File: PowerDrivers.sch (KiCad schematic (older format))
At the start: 58 parts, among them P2 GOOSVN, P3 GOOSVN, P4 GOOSVN, P5 GOOSVN, P6 GOOSVN, P7 GOOSVN, P8 GOOSVN, P9 GOOSVN, Q1 PSMN6R0-30YLB, Q2 PSMN6R0-30YLB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

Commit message: Finished schematics
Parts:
- removed C14: C, symbol C
- removed P3: GOOSVN, symbol CONN_01X02
- removed Q2: PSMN6R0-30YLB, symbol Q_NMOS_SSSGD
- removed R3: 470k, symbol R
- removed R5: 10k, symbol R
- added C7: 10u/25V, Capacitors_SMD:C_0805, symbol C
- added P10: GS009S, Connect:AK300-2, symbol CONN_01X02
- added Q9: PSMN6R0, SMD_Packages:SO-8_PowerPAK_Vishay_Single, symbol Q_NMOS_SSSGD
- added R18: 10k, Resistors_SMD:R_0603, symbol R
- added R4: 560k, Resistors_SMD:R_0603, symbol R
- C10, C11, C12, C13, C8, C9: value C -> 10u/25V; footprint (none) -> Capacitors_SMD:C_0805; Alt. Order Code (none) -> 302010178; Alt. Supplier (none) -> Open Parts Library; Manufacturer (none) -> Yageo; Note (none) -> 10μF/25V 0805 X5R ceramic capacitor; Order Code (none) -> 1735530; Package (none) -> 0805; Part Number (none) -> CC0805KKX5R8BB106; Supplier (none) -> Farnell
- C14: renamed from C15; footprint (none) -> Capacitors_SMD:C_0805; Alt. Order Code (none) -> 302010178; Alt. Supplier (none) -> Open Parts Library; Manufacturer (none) -> Yageo; Note (none) -> 10μF/25V 0805 X5R ceramic capacitor; Order Code (none) -> 1735530; Package (none) -> 0805; Part Number (none) -> CC0805KKX5R8BB106
- C6: renamed from C?; footprint (none) -> Capacitors_SMD:C_0603
- D1: footprint (none) -> LEDs:LED_0603; Alt. Order Code (none) -> 304090043; Alt. Supplier (none) -> Open Parts Library; Manufacturer (none) -> Everlight; Note (none) -> Green 0603 LED; Order Code (none) -> 8554609; Package (none) -> 0603
- D10, D13, D14, D2, D5, D6, D9: value LED -> LED GREEN; footprint (none) -> LEDs:LED_0603; Alt. Order Code (none) -> 304090043; Alt. Supplier (none) -> Open Parts Library; Manufacturer (none) -> Everlight; Note (none) -> Green 0603 LED; Order Code (none) -> 8554609; Package (none) -> 0603; Part Number (none) -> 19-217-G7C-AN1P2-3T; Supplier (none) -> Farnell
- D11, D12, D15, D16, D3, D4, D7, D8: footprint (none) -> Diodes_SMD:SMA_Standard; Alt. Order Code (none) -> 304020027; Alt. Supplier (none) -> Open Parts Library; Manufacturer (none) -> Diodes; Note (none) -> Schottky rectifier 40 V 1 A SOD-123; Order Code (none) -> 1773475; Package (none) -> DO-214AC; Part Number (none) -> 1N5819HW-7-F; Supplier (none) -> Farnell
- P3: renamed from P2; value GOOSVN -> GS009S; footprint (none) -> Connect:AK300-2; Alt. Order Code (none) -> 320110028; Alt. Supplier (none) -> Open Parts Library; Manufacturer (none) -> GOOSVN; Note (none) -> 5mm 2way screw terminal; Order Code (none) -> 2493622; Package (none) -> 5mm pitch; Part Number (none) -> GS009S-5.0-02P-1; Supplier (none) -> Farnell
- P4, P5, P6, P7, P8, P9: value GOOSVN -> GS009S; footprint (none) -> Connect:AK300-2; Alt. Order Code (none) -> 320110028; Alt. Supplier (none) -> Open Parts Library; Manufacturer (none) -> GOOSVN; Note (none) -> 5mm 2way screw terminal; Order Code (none) -> 2493622; Package (none) -> 5mm pitch; Part Number (none) -> GS009S-5.0-02P-1; Supplier (none) -> Farnell
- Q2: renamed from Q1; value PSMN6R0-30YLB -> PSMN6R0; footprint (none) -> SMD_Packages:SO-8_PowerPAK_Vishay_Single; Manufacturer (none) -> NXP; Note (none) -> N-channel 30V 70A LFPAK MOSFET; Order Code (none) -> 2067550; Package (none) -> Power-SO8; Part Number (none) -> PSMN6R0-30YLB
- Q3, Q4, Q5, Q6, Q7, Q8: value PSMN6R0-30YLB -> PSMN6R0; footprint (none) -> SMD_Packages:SO-8_PowerPAK_Vishay_Single; Manufacturer (none) -> NXP; Note (none) -> N-channel 30V 70A LFPAK MOSFET; Order Code (none) -> 2067550; Package (none) -> Power-SO8; Part Number (none) -> PSMN6R0-30YLB
- R10, R14, R6: value 470k -> 10k; footprint (none) -> Resistors_SMD:R_0603; Alt. Order Code (none) -> 301010299; Alt. Supplier (none) -> Open Parts Library; Manufacturer (none) -> Yageo; Note (none) -> 10kΩ/1% 0603 resistor; Order Code (none) -> 9238603; Package (none) -> 0603; Part Number (none) -> RC0603FR-0710KL; Supplier (none) -> Farnell
- R11, R15, R7: value 470k -> 560k; footprint (none) -> Resistors_SMD:R_0603; Alt. Order Code (none) -> 301010230; Alt. Supplier (none) -> Open Parts Library; Manufacturer (none) -> Yageo; Note (none) -> 560kΩ/5% 0603 resistor; Order Code (none) -> 9233717; Package (none) -> 0603; Part Number (none) -> RC0603JR-07560KL; Supplier (none) -> Farnell
- R12, R16, R8: value 10k -> 560k; footprint (none) -> Resistors_SMD:R_0603; Alt. Order Code (none) -> 301010230; Alt. Supplier (none) -> Open Parts Library; Manufacturer (none) -> Yageo; Note (none) -> 560kΩ/5% 0603 resistor; Order Code (none) -> 9233717; Package (none) -> 0603; Part Number (none) -> RC0603JR-07560KL
- R13, R17, R9: footprint (none) -> Resistors_SMD:R_0603; Alt. Order Code (none) -> 301010299; Alt. Supplier (none) -> Open Parts Library; Manufacturer (none) -> Yageo; Note (none) -> 10kΩ/1% 0603 resistor; Order Code (none) -> 9238603; Package (none) -> 0603; Part Number (none) -> RC0603FR-0710KL
- R3: renamed from R2; value 470k -> 560k; footprint (none) -> Resistors_SMD:R_0603; Alt. Order Code (none) -> 301010230; Alt. Supplier (none) -> Open Parts Library; Manufacturer (none) -> Yageo; Note (none) -> 560kΩ/5% 0603 resistor; Order Code (none) -> 9233717; Package (none) -> 0603; Part Number (none) -> RC0603JR-07560KL; Supplier (none) -> Farnell
- R5: renamed from R4; footprint (none) -> Resistors_SMD:R_0603; Alt. Order Code (none) -> 301010299; Alt. Supplier (none) -> Open Parts Library; Manufacturer (none) -> Yageo; Note (none) -> 10kΩ/1% 0603 resistor; Order Code (none) -> 9238603; Package (none) -> 0603; Part Number (none) -> RC0603FR-0710KL
- U3: renamed from U4; footprint (none) -> Housings_SSOP:TSSOP-20_4.4x6.5mm_Pitch0.65mm; Package TSSOP-16 -> TSSOP-20

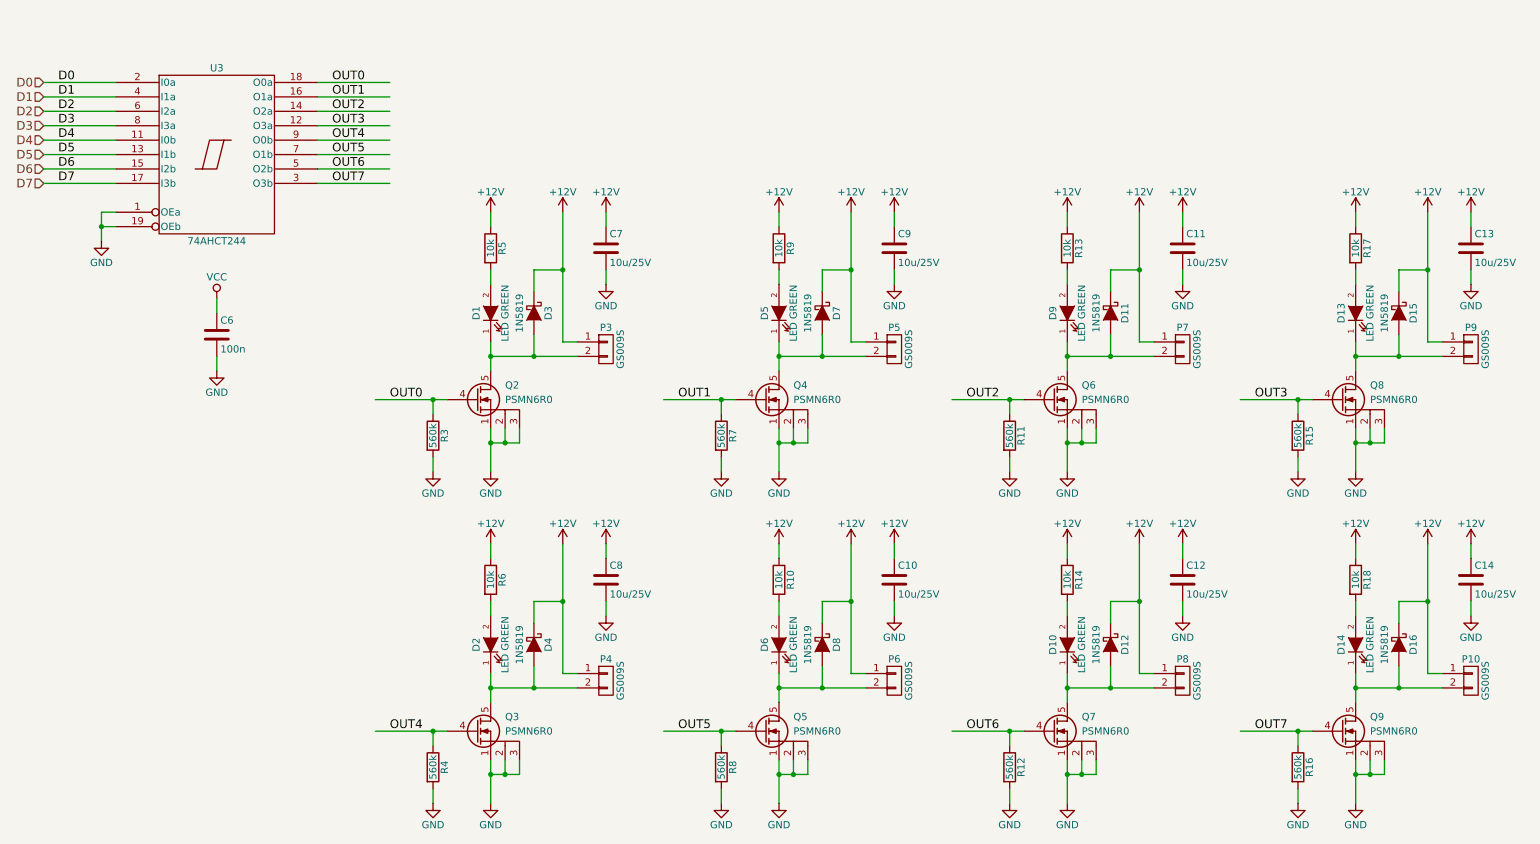
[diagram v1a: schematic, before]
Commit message: Laid out parts and routed some of the signals
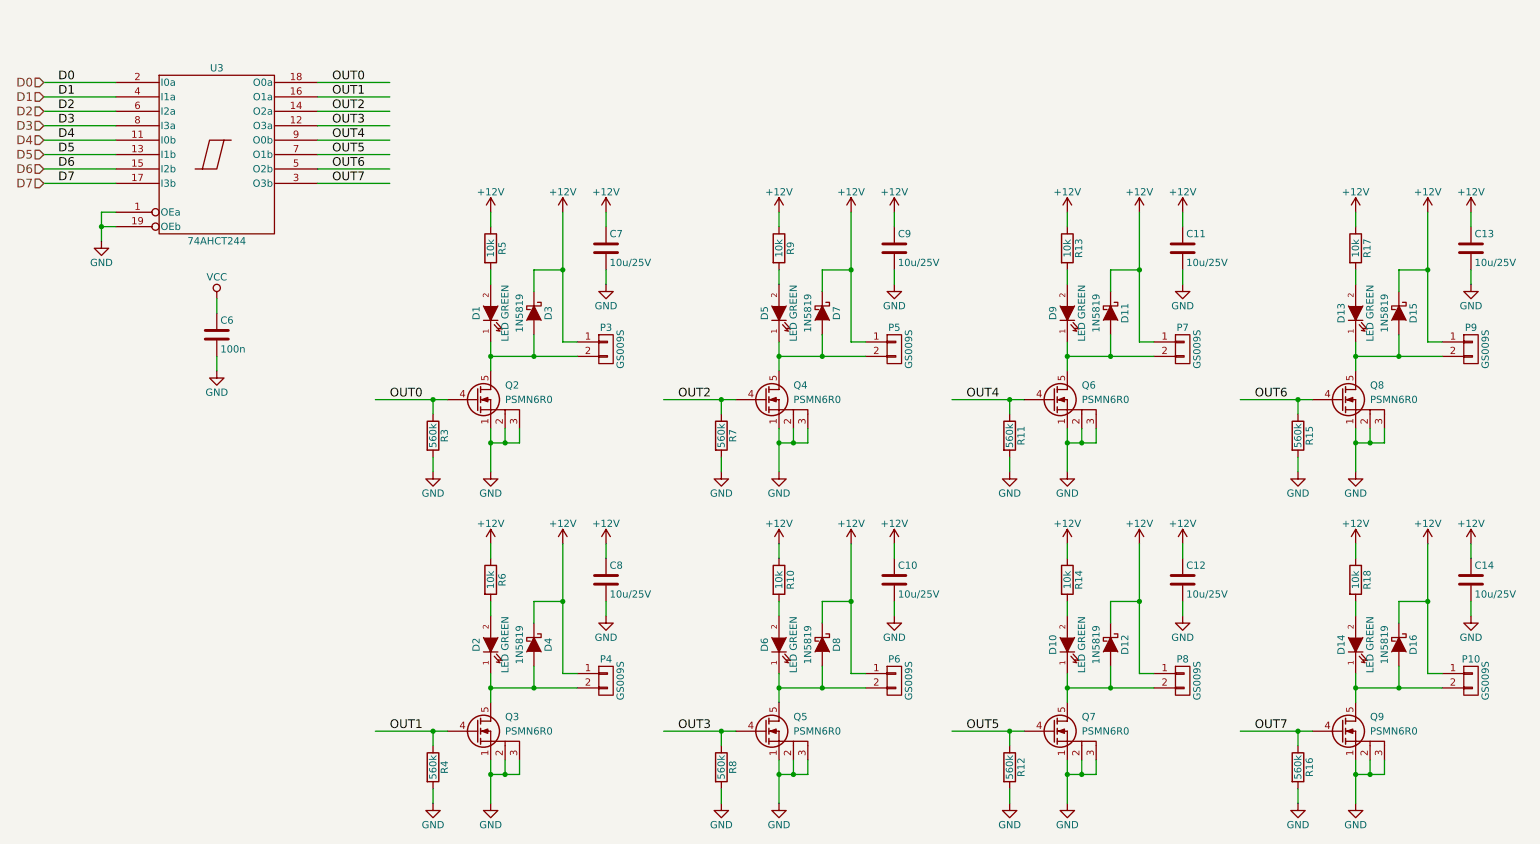
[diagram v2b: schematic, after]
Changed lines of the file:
@@
 Connection ~ 5700 3300
 Text Label 5400 3300 0    60   ~ 0
-OUT1
+OUT2
 Wire Wire Line
 	7700 3400 7700 3300
@@
 Connection ~ 7700 3300
 Text Label 7400 3300 0    60   ~ 0
-OUT2
+OUT4
 Wire Wire Line
 	9700 3400 9700 3300
@@
 Connection ~ 9700 3300
 Text Label 9400 3300 0    60   ~ 0
-OUT3
+OUT6
 Wire Wire Line
 	3700 5700 3700 5600
@@
 Connection ~ 3700 5600
 Text Label 3400 5600 0    60   ~ 0
-OUT4
+OUT1
 Wire Wire Line
 	5700 5700 5700 5600
@@
 Connection ~ 5700 5600
 Text Label 5400 5600 0    60   ~ 0
-OUT5
+OUT3
 Wire Wire Line
 	7700 5700 7700 5600
@@
 Connection ~ 7700 5600
 Text Label 7400 5600 0    60   ~ 0
-OUT6
+OUT5
 Wire Wire Line
 	9700 5700 9700 5600

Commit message: Final production board
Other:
- note added: "3.3V-TO-5V LEVEL SHIFTER"
- note added: "EIGHT INDEPENDENT HIGH-CURRENT MOSFET DRIVERS"
- note added: "POWER DRIVERS\nUp to eight external devices can be connected and controlled by the unit.\nEach device is controlled by a separate MOSFET and supplied by a 12V DC power supply.\nPWM can be employed to vary the power to the device, such as a solenoid valve or LED lightning.\nThere is a level shifter to convert the 3.3V Aurduino outputs to 5 Volts to efficiently drive the gates of the MOSFET transis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"
- moved on the sheet: C6, U3
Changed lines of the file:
@@
 LIBS:valves
 LIBS:jakub
-LIBS:garduino-cache
+LIBS:guarduino-cache
 EELAYER 25 0
 EELAYER END
@@
 encoding utf-8
 Sheet 2 4
-Title ""
-Date ""
-Rev ""
-Comp ""
-Comment1 ""
-Comment2 ""
+Title "Guarduino Control Unit"
+Date "2016-09-30"
+Rev "1.0"
+Comp "Serious Play Ltd"
+Comment1 "Jakub Nedbal"
+Comment2 "License: CC-BY-SA"
 Comment3 ""
 Comment4 ""
@@
 Connection ~ 5700 3300
 Text Label 5400 3300 0    60   ~ 0
-OUT2
+OUT1
 Wire Wire Line
 	7700 3400 7700 3300
@@
 Connection ~ 7700 3300
 Text Label 7400 3300 0    60   ~ 0
-OUT4
+OUT2
 Wire Wire Line
 	9700 3400 9700 3300
@@
 Connection ~ 9700 3300
 Text Label 9400 3300 0    60   ~ 0
-OUT6
+OUT3
 Wire Wire Line
 	3700 5700 3700 5600
@@
 Connection ~ 3700 5600
 Text Label 3400 5600 0    60   ~ 0
-OUT1
+OUT4
 Wire Wire Line
 	5700 5700 5700 5600
@@
 Connection ~ 5700 5600
 Text Label 5400 5600 0    60   ~ 0
-OUT3
+OUT5
 Wire Wire Line
 	7700 5700 7700 5600
@@
 Connection ~ 7700 5600
 Text Label 7400 5600 0    60   ~ 0
-OUT5
+OUT6
 Wire Wire Line
 	9700 5700 9700 5600
@@
 L 74LS244 U3
 U 1 1 570B4B9F
-P 2200 1600
-F 0 "U3" H 2200 2200 50  0000 C CNN
-F 1 "74AHCT244" H 2200 1000 50  0000 C CNN
-F 2 "Housings_SSOP:TSSOP-20_4.4x6.5mm_Pitch0.65mm" H 2200 1600 50  0001 C CNN
-F 3 "" H 2200 1600 50  0000 C CNN
-F 4 "SN74AHCT244PW" H 2200 1600 60  0001 C CNN "Part Number"
-F 5 "Texas Instruments" H 2200 1600 60  0001 C CNN "Manufacturer"
-F 6 "TSSOP-20" H 2200 1600 60  0001 C CNN "Package"
-F 7 "Farnell" H 2200 1600 60  0001 C CNN "Supplier"
-F 8 "9590706" H 2200 1600 60  0001 C CNN "Order Code"
-F 9 "Octal buffers/drivers with 3-state outputs" H 2200 1600 60  0001 C CNN "Note"
-	1    2200 1600
-	1    0    0    -1
-$EndComp
-Wire Wire Line
-	1500 1100 1000 1100
-Text Label 1100 1100 0    60   ~ 0
+P 2200 2400
+F 0 "U3" H 2200 3000 50  0000 C CNN
+F 1 "74AHCT244" H 2200 1800 50  0000 C CNN
+F 2 "Housings_SSOP:TSSOP-20_4.4x6.5mm_Pitch0.65mm" H 2200 2400 50  0001 C CNN
+F 3 "" H 2200 2400 50  0000 C CNN
+F 4 "SN74AHCT244PW" H 2200 2400 60  0001 C CNN "Part Number"
+F 5 "Texas Instruments" H 2200 2400 60  0001 C CNN "Manufacturer"
+F 6 "TSSOP-20" H 2200 2400 60  0001 C CNN "Package"
+F 7 "Farnell" H 2200 2400 60  0001 C CNN "Supplier"
+F 8 "9590706" H 2200 2400 60  0001 C CNN "Order Code"
+F 9 "Octal buffers/drivers with 3-state outputs" H 2200 2400 60  0001 C CNN "Note"
+	1    2200 2400
+	1    0    0    -1
+$EndComp
+Wire Wire Line
+	1500 1900 1000 1900
+Text Label 1100 1900 0    60   ~ 0
 D0
 Wire Wire Line
-	1500 1200 1000 1200
-Text Label 1100 1200 0    60   ~ 0
+	1500 2000 1000 2000
+Text Label 1100 2000 0    60   ~ 0
 D1
 Wire Wire Line
-	1500 1300 1000 1300
-Text Label 1100 1300 0    60   ~ 0
+	1500 2100 1000 2100
+Text Label 1100 2100 0    60   ~ 0
 D2
 Wire Wire Line
-	1500 1400 1000 1400
-Text Label 1100 1400 0    60   ~ 0
+	1500 2200 1000 2200
+Text Label 1100 2200 0    60   ~ 0
 D3
 Wire Wire Line
-	1500 1500 1000 1500
-Text Label 1100 1500 0    60   ~ 0
+	1500 2300 1000 2300
+Text Label 1100 2300 0    60   ~ 0
 D4
 Wire Wire Line
-	1500 1600 1000 1600
-Text Label 1100 1600 0    60   ~ 0
+	1500 2400 1000 2400
+Text Label 1100 2400 0    60   ~ 0
 D5
 Wire Wire Line
-	1500 1700 1000 1700
-Text Label 1100 1700 0    60   ~ 0
+	1500 2500 1000 2500
+Text Label 1100 2500 0    60   ~ 0
 D6
 Wire Wire Line
-	1500 1800 1000 1800
-Text Label 1100 1800 0    60   ~ 0
+	1500 2600 1000 2600
+Text Label 1100 2600 0    60   ~ 0
 D7
 Wire Wire Line
-	1500 2000 1400 2000
-Wire Wire Line
-	1400 2000 1400 2200
-Wire Wire Line
-	1400 2100 1500 2100
-Connection ~ 1400 2100
+	1500 2800 1400 2800
+Wire Wire Line
+	1400 2800 1400 3000
+Wire Wire Line
+	1400 2900 1500 2900
+Connection ~ 1400 2900
 $Comp
 L GND #PWR058
 U 1 1 570B4BBA
-P 1400 2200
-F 0 "#PWR058" H 1400 1950 50  0001 C CNN
-F 1 "GND" H 1400 2050 50  0000 C CNN
-F 2 "" H 1400 2200 50  0000 C CNN
-F 3 "" H 1400 2200 50  0000 C CNN
-	1    1400 2200
-	1    0    0    -1
-$EndComp
-Wire Wire Line
-	3400 1100 2900 1100
-Text Label 3000 1100 0    60   ~ 0
+P 1400 3000
+F 0 "#PWR058" H 1400 2750 50  0001 C CNN
+F 1 "GND" H 1400 2850 50  0000 C CNN
+F 2 "" H 1400 3000 50  0000 C CNN
+F 3 "" H 1400 3000 50  0000 C CNN
+	1    1400 3000
+	1    0    0    -1
+$EndComp
+Wire Wire Line
+	3400 1900 2900 1900
+Text Label 3000 1900 0    60   ~ 0
 OUT0
 Wire Wire Line
-	3400 1200 2900 1200
-Text Label 3000 1200 0    60   ~ 0
+	3400 2000 2900 2000
+Text Label 3000 2000 0    60   ~ 0
 OUT1
 Wire Wire Line
-	3400 1300 2900 1300
-Text Label 3000 1300 0    60   ~ 0
+	3400 2100 2900 2100
+Text Label 3000 2100 0    60   ~ 0
 OUT2
 Wire Wire Line
-	3400 1400 2900 1400
-Text Label 3000 1400 0    60   ~ 0
+	3400 2200 2900 2200
+Text Label 3000 2200 0    60   ~ 0
 OUT3
 Wire Wire Line
-	3400 1500 2900 1500
-Text Label 3000 1500 0    60   ~ 0
+	3400 2300 2900 2300
+Text Label 3000 2300 0    60   ~ 0
 OUT4
 Wire Wire Line
-	3400 1600 2900 1600
-Text Label 3000 1600 0    60   ~ 0
+	3400 2400 2900 2400
+Text Label 3000 2400 0    60   ~ 0
 OUT5
 Wire Wire Line
-	3400 1700 2900 1700
-Text Label 3000 1700 0    60   ~ 0
+	3400 2500 2900 2500
+Text Label 3000 2500 0    60   ~ 0
 OUT6
 Wire Wire Line
-	3400 1800 2900 1800
-Text Label 3000 1800 0    60   ~ 0
+	3400 2600 2900 2600
+Text Label 3000 2600 0    60   ~ 0
 OUT7
-Text HLabel 1000 1100 0    60   Input ~ 0
+Text HLabel 1000 1900 0    60   Input ~ 0
 D0
-Text HLabel 1000 1200 0    60   Input ~ 0
+Text HLabel 1000 2000 0    60   Input ~ 0
 D1
-Text HLabel 1000 1300 0    60   Input ~ 0
+Text HLabel 1000 2100 0    60   Input ~ 0
 D2
-Text HLabel 1000 1400 0    60   Input ~ 0
+Text HLabel 1000 2200 0    60   Input ~ 0
 D3
-Text HLabel 1000 1500 0    60   Input ~ 0
+Text HLabel 1000 2300 0    60   Input ~ 0
 D4
-Text HLabel 1000 1600 0    60   Input ~ 0
+Text HLabel 1000 2400 0    60   Input ~ 0
 D5
-Text HLabel 1000 1700 0    60   Input ~ 0
+Text HLabel 1000 2500 0    60   Input ~ 0
 D6
-Text HLabel 1000 1800 0    60   Input ~ 0
+Text HLabel 1000 2600 0    60   Input ~ 0
 D7
 Wire Wire Line
-	2200 3000 2200 3100
+	2200 3800 2200 3900
 $Comp
 L GND #PWR059
 U 1 1 570C5201
-P 2200 3100
-F 0 "#PWR059" H 2200 2850 50  0001 C CNN
-F 1 "GND" H 2200 2950 50  0000 C CNN
-F 2 "" H 2200 3100 50  0000 C CNN
-F 3 "" H 2200 3100 50  0000 C CNN
-	1    2200 3100
-	1    0    0    -1
-$EndComp
-Wire Wire Line
-	2200 2700 2200 2600
+P 2200 3900
+F 0 "#PWR059" H 2200 3650 50  0001 C CNN
+F 1 "GND" H 2200 3750 50  0000 C CNN
+F 2 "" H 2200 3900 50  0000 C CNN
+F 3 "" H 2200 3900 50  0000 C CNN
+	1    2200 3900
+	1    0    0    -1
+$EndComp
+Wire Wire Line
+	2200 3500 2200 3400
 $Comp
 L VCC #PWR060
 U 1 1 570C52A7
-P 2200 2600
-F 0 "#PWR060" H 2200 2450 50  0001 C CNN
-F 1 "VCC" H 2200 2750 50  0000 C CNN
-F 2 "" H 2200 2600 50  0000 C CNN
-F 3 "" H 2200 2600 50  0000 C CNN
-	1    2200 2600
+P 2200 3400
+F 0 "#PWR060" H 2200 3250 50  0001 C CNN
+F 1 "VCC" H 2200 3550 50  0000 C CNN
+F 2 "" H 2200 3400 50  0000 C CNN
+F 3 "" H 2200 3400 50  0000 C CNN
+	1    2200 3400
 	1    0    0    -1
 $EndComp
@@
 L C C6
 U 1 1 57490CEE
-P 2200 2850
-F 0 "C6" H 2225 2950 50  0000 L CNN
-F 1 "100n" H 2225 2750 50  0000 L CNN
-F 2 "Capacitors_SMD:C_0603" H 2238 2700 50  0001 C CNN
-F 3 "" H 2200 2850 50  0000 C CNN
-F 4 "CC0603KRX7R9BB104" H 2200 2850 60  0001 C CNN "Part Number"
-F 5 "Yageo" H 2200 2850 60  0001 C CNN "Manufacturer"
-F 6 "0603" H 2200 2850 60  0001 C CNN "Package"
-F 7 "Farnell" H 2200 2850 60  0001 C CNN "Supplier"
-F 8 "1362556" H 2200 2850 60  0001 C CNN "Order Code"
-F 9 "Open Parts Library" H 2200 2850 60  0001 C CNN "Alt. Supplier"
-F 10 "302010138" H 2200 2850 60  0001 C CNN "Alt. Order Code"
-F 11 "100nF/50V X7R 0603 ceramic capacitor" H 2200 2850 60  0001 C CNN "Note"
-	1    2200 2850
+P 2200 3650
+F 0 "C6" H 2225 3750 50  0000 L CNN
+F 1 "100n" H 2225 3550 50  0000 L CNN
+F 2 "Capacitors_SMD:C_0603" H 2238 3500 50  0001 C CNN
+F 3 "" H 2200 3650 50  0000 C CNN
+F 4 "CC0603KRX7R9BB104" H 2200 3650 60  0001 C CNN "Part Number"
+F 5 "Yageo" H 2200 3650 60  0001 C CNN "Manufacturer"
+F 6 "0603" H 2200 3650 60  0001 C CNN "Package"
+F 7 "Farnell" H 2200 3650 60  0001 C CNN "Supplier"
+F 8 "1362556" H 2200 3650 60  0001 C CNN "Order Code"
+F 9 "Open Parts Library" H 2200 3650 60  0001 C CNN "Alt. Supplier"
+F 10 "302010138" H 2200 3650 60  0001 C CNN "Alt. Order Code"
+F 11 "100nF/50V X7R 0603 ceramic capacitor" H 2200 3650 60  0001 C CNN "Note"
+	1    2200 3650
 	1    0    0    -1
 $EndComp
@@
 	1    0    0    -1
 $EndComp
+Text Notes 800  1100 0    60   ~ 0
+POWER DRIVERS\nUp to eight external devices can be connected and controlled by the unit.\nEach device is controlled by a separate MOSFET and supplied by a 12V DC power supply.\nPWM can be employed to vary the power to the device, such as a solenoid valve or LED lightning.\nThere is a level shifter to convert the 3.3V Aurduino outputs to 5 Volts to efficiently drive the gates of the MOSFET transistors.
+Text Notes 5900 1600 0    60   ~ 0
+EIGHT INDEPENDENT HIGH-CURRENT MOSFET DRIVERS
+Text Notes 1600 1600 0    60   ~ 0
+3.3V-TO-5V LEVEL SHIFTER
 $EndSCHEMATC
